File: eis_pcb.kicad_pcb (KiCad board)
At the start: 6 copper layers, 36 x 37.5 mm, 94 parts, among them J1 541020164, J2 104031-0811, J3 527451897, J4 GSB1C41110SSHR, P1 +BATT, P2 GND, P3 DATA+, P4 DATA-, P5 RXD0, P6 TXD0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

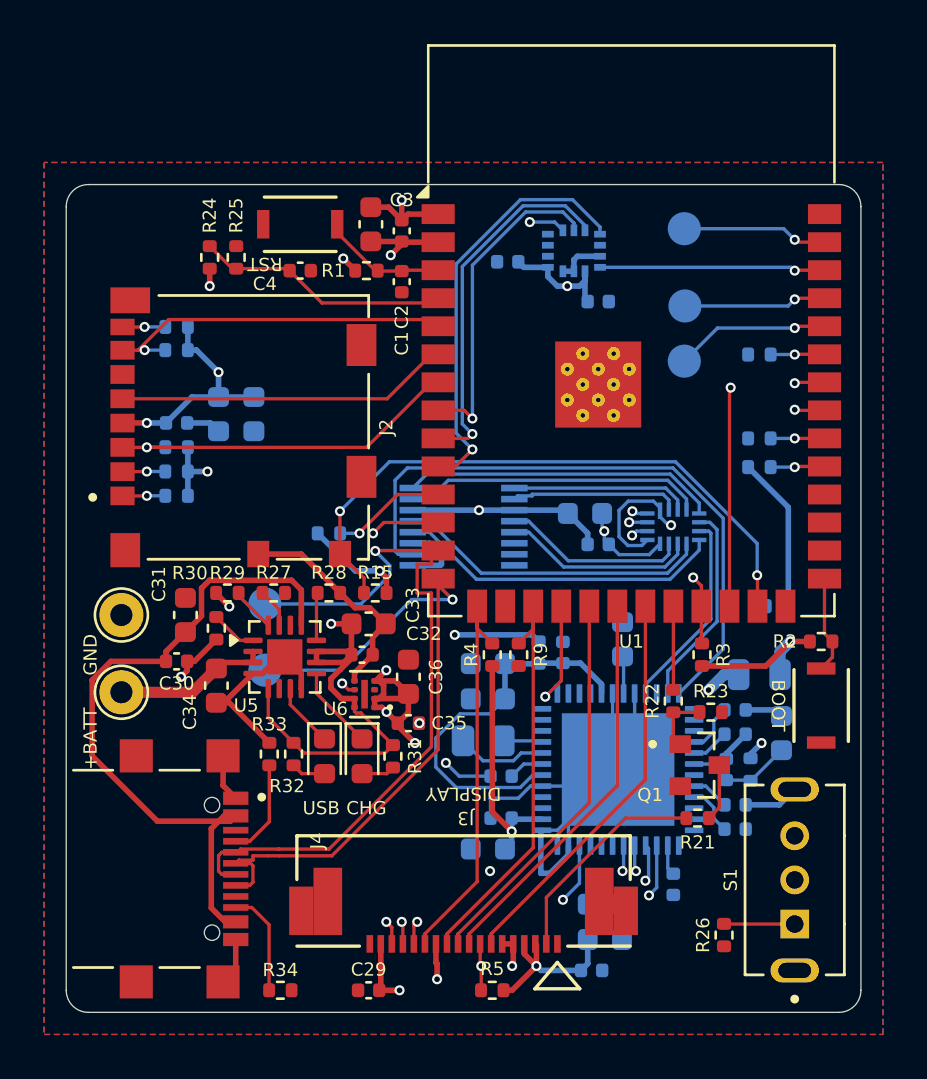
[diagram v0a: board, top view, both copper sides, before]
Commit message: fix drc/net errors, add via stitching
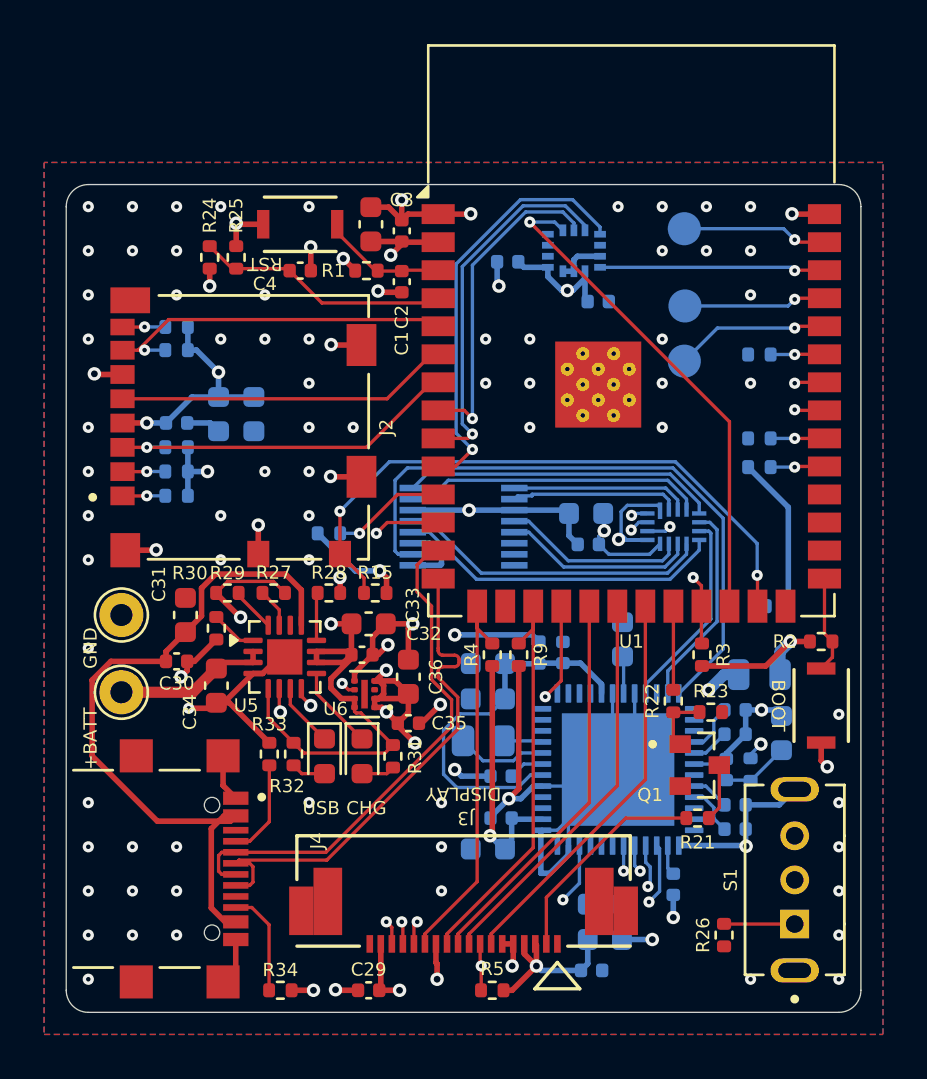
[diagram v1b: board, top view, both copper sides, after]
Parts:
- removed the P3 at (109.0, 102.0)
- removed the P4 at (109.0, 99.0)
- moved C19 0.45 mm to (123.7, 96.3)
- renumbered P5 to P3, P6 to P4, P7 to P5
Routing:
- net GND: track 91.9 -> 130.7 mm, vias 10 -> 102
- net /DATA-: track 34.0 -> 23.7 mm, vias 1 -> 0
- net /DATA+: track 32.6 -> 23.7 mm, vias 1 -> 0
- net /A1.MUX: track 12.2 -> 10.3 mm
- net /CS.IMU: track 23.8 -> 22.8 mm, vias 2 -> 1
- net +3V3: track 76.8 -> 77.6 mm
- net /3V3A: track 9.81 -> 10.6 mm
- net /CS.AFE: track 27.0 -> 27.7 mm
- net /SCLK: track 46.1 -> 46.6 mm
